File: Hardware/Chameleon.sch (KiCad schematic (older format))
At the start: 59 parts, among them IC1 ATTINY44-SS, P1 CONN_3X2, U1 PCA9685, U2 USBMICRO-B, U3 NCP1402, X1 CRYSTAL

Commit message: Added I2C series resistors, updated Project Log, added PDF version of Project Log
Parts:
- added R22, R3: 1.5k, symbol R
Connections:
- wire segments 236 -> 238
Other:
- moved on the sheet: R1, R2

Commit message: Updated schematics and Project Log with new resistor values, and added PDF BOM
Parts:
- R1, R2: value 1.5k -> 1.8k
- R22, R3: value 1.5k -> 100
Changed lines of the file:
@@
-EESchema Schematic File Version 2  date 8/27/2012 9:40:04 PM
+EESchema Schematic File Version 2  date 9/9/2012 6:02:59 PM
 LIBS:power
 LIBS:device
@@
 Sheet 1 1
 Title "Chameleon Drink Coasters"
-Date "28 aug 2012"
+Date "9 sep 2012"
 Rev "1.0"
 Comp "Projects and Stuff LLC"
@@
 P 950 5550
 F 0 "R3" V 1050 5550 50  0000 C CNN
-F 1 "1.5k" V 950 5550 50  0000 C CNN
+F 1 "100" V 950 5550 50  0000 C CNN
 	1    950  5550
 	0    1    1    0
@@
 P 1000 5450
 F 0 "R22" V 1080 5450 50  0000 C CNN
-F 1 "1.5k" V 1000 5450 50  0000 C CNN
+F 1 "100" V 1000 5450 50  0000 C CNN
 	1    1000 5450
 	0    -1   -1   0
@@
 P 1300 5050
 F 0 "R1" V 1380 5050 50  0000 C CNN
-F 1 "1.5k" V 1300 5050 50  0000 C CNN
+F 1 "1.8k" V 1300 5050 50  0000 C CNN
 	1    1300 5050
 	-1   0    0    1
@@
 P 1450 5050
 F 0 "R2" V 1530 5050 50  0000 C CNN
-F 1 "1.5k" V 1450 5050 50  0000 C CNN
+F 1 "1.8k" V 1450 5050 50  0000 C CNN
 	1    1450 5050
 	-1   0    0    1
@@
 6E 56 52 49 51 4E 59 71 7E 65 C5 4D 0F AF 00 BF F6 21 9D BA 45 88 9C 00 16 00 C0 66 90 E0 00 00
 AC 42 3B 38 00 00 AB 90 E0 00 00 AC 42 82 03 00 B0 EA FF 00 E3 76 B5 A7 81 B6 BC 08 00 00 00 00
-49 45 4E 44 AE 42 60 82 4E $EndBitmap
+49 45 4E 44 AE 42 60 82 38 $EndBitmap
 EndData
 $EndBitmap

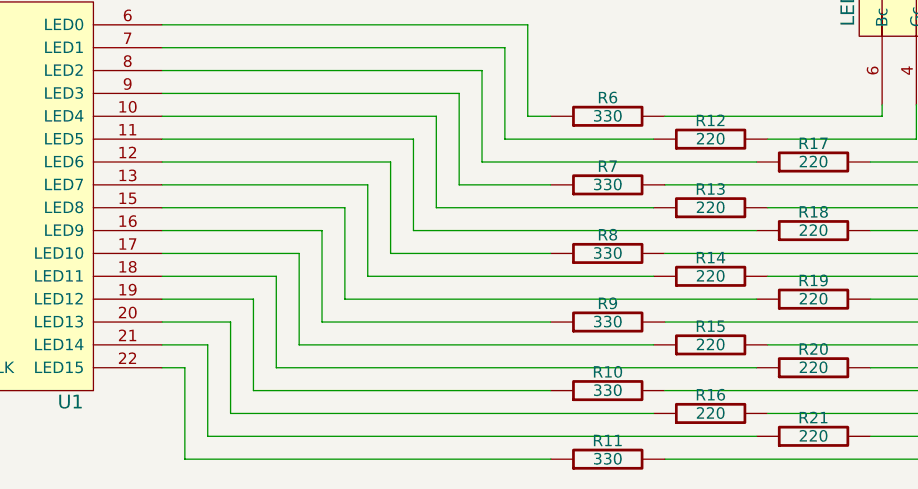
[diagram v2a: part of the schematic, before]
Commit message: Routed board (with LEDs corrected) and updated Project Log
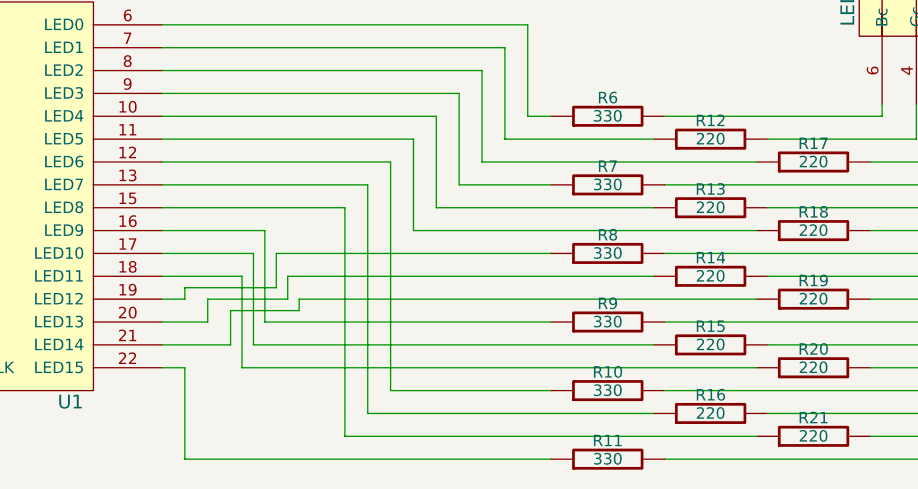
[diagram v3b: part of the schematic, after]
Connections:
- wire segments 238 -> 244
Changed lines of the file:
@@
-EESchema Schematic File Version 2  date 9/9/2012 6:02:59 PM
+EESchema Schematic File Version 2  date 12/30/2012 6:35:34 PM
 LIBS:power
 LIBS:device
@@
 Sheet 1 1
 Title "Chameleon Drink Coasters"
-Date "9 sep 2012"
+Date "30 dec 2012"
 Rev "1.0"
 Comp "Projects and Stuff LLC"
@@
 $EndDescr
 Wire Wire Line
+	4700 6850 3100 6850
+Wire Wire Line
+	5600 6750 3800 6750
+Wire Wire Line
+	3800 6750 3800 5750
+Wire Wire Line
+	3800 5750 3000 5750
+Wire Wire Line
+	3000 5550 4000 5550
+Wire Wire Line
+	4000 5550 4000 6550
+Wire Wire Line
+	4000 6550 4700 6550
+Wire Wire Line
+	5150 6050 3550 6050
+Wire Wire Line
+	3550 6050 3550 6150
+Wire Wire Line
+	3550 6150 3200 6150
+Wire Wire Line
+	3200 6150 3200 6250
+Wire Wire Line
+	5600 6450 3350 6450
+Wire Wire Line
+	3350 6450 3350 6050
+Wire Wire Line
+	3350 6050 3000 6050
+Wire Wire Line
+	3000 5850 3450 5850
+Wire Wire Line
+	3450 5850 3450 6250
+Wire Wire Line
+	3450 6250 4700 6250
+Wire Wire Line
+	3000 6150 3100 6150
+Wire Wire Line
 	600  5550 700  5550
 Wire Wire Line
@@
 	1700 6250 1750 6250
 Wire Wire Line
-	3000 6450 3100 6450
-Wire Wire Line
-	3100 6450 3100 6850
-Wire Wire Line
-	3100 6850 4700 6850
-Wire Wire Line
 	10300 3600 10300 4500
 Wire Wire Line
@@
 	6300 5450 5650 5450
 Wire Wire Line
-	3000 6050 3500 6050
-Wire Wire Line
-	3000 5850 3700 5850
-Wire Wire Line
-	3000 5650 3900 5650
-Wire Wire Line
 	3000 5450 4100 5450
 Wire Wire Line
@@
 Wire Wire Line
 	3000 5050 4500 5050
-Wire Wire Line
-	3000 6150 3400 6150
-Wire Wire Line
-	3000 6350 3200 6350
-Wire Wire Line
-	3300 6650 3300 6250
-Wire Wire Line
-	3300 6650 5150 6650
-Wire Wire Line
-	3500 6050 3500 6450
-Wire Wire Line
-	3500 6450 5600 6450
-Wire Wire Line
-	3700 5850 3700 6250
-Wire Wire Line
-	3700 6250 4700 6250
-Wire Wire Line
-	5150 6050 3900 6050
-Wire Wire Line
-	3900 6050 3900 5650
 Wire Wire Line
 	5600 5850 4100 5850
@@
 	4200 5750 5150 5750
 Wire Wire Line
-	4000 5950 4000 5550
-Wire Wire Line
-	4000 5950 4700 5950
-Wire Wire Line
-	3800 6150 3800 5750
-Wire Wire Line
-	3800 6150 5600 6150
-Wire Wire Line
-	5150 6350 3600 6350
-Wire Wire Line
-	3600 6350 3600 5950
-Wire Wire Line
-	4700 6550 3400 6550
-Wire Wire Line
-	3400 6550 3400 6150
-Wire Wire Line
-	5600 6750 3200 6750
-Wire Wire Line
-	3200 6750 3200 6350
-Wire Wire Line
-	3300 6250 3000 6250
-Wire Wire Line
 	4600 4950 3000 4950
 Wire Wire Line
@@
 Wire Wire Line
 	4200 5350 3000 5350
-Wire Wire Line
-	4000 5550 3000 5550
-Wire Wire Line
-	3800 5750 3000 5750
-Wire Wire Line
-	3600 5950 3000 5950
 Wire Wire Line
 	6150 5350 5200 5350
@@
 Wire Wire Line
 	1200 5550 1750 5550
+Wire Wire Line
+	3200 6250 3000 6250
+Wire Wire Line
+	3000 6350 3300 6350
+Wire Wire Line
+	3000 5950 3400 5950
+Wire Wire Line
+	3400 5950 3400 6350
+Wire Wire Line
+	3400 6350 5150 6350
+Wire Wire Line
+	4700 5950 3500 5950
+Wire Wire Line
+	3500 5950 3500 6100
+Wire Wire Line
+	3500 6100 3100 6100
+Wire Wire Line
+	3100 6100 3100 6150
+Wire Wire Line
+	3300 6350 3300 6200
+Wire Wire Line
+	3300 6200 3600 6200
+Wire Wire Line
+	3600 6200 3600 6150
+Wire Wire Line
+	3600 6150 5600 6150
+Wire Wire Line
+	5150 6650 3900 6650
+Wire Wire Line
+	3900 6650 3900 5650
+Wire Wire Line
+	3900 5650 3000 5650
+Wire Wire Line
+	3100 6850 3100 6450
+Wire Wire Line
+	3100 6450 3000 6450
 Text Label 600  5550 1    60   ~ 0
 MOSI
@@
 6E 56 52 49 51 4E 59 71 7E 65 C5 4D 0F AF 00 BF F6 21 9D BA 45 88 9C 00 16 00 C0 66 90 E0 00 00
 AC 42 3B 38 00 00 AB 90 E0 00 00 AC 42 82 03 00 B0 EA FF 00 E3 76 B5 A7 81 B6 BC 08 00 00 00 00
-49 45 4E 44 AE 42 60 82 38 $EndBitmap
+49 45 4E 44 AE 42 60 82 89 $EndBitmap
 EndData
 $EndBitmap

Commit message: Began transitioning to updated Parts to improve function and increase capability.
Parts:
- removed C4, C5: 8pF, symbol CSMALL
- removed X1: CRYSTAL, symbol CRYSTAL
- added F?: FUSE, ~, symbol FUSE
- added IC?: ATXMEGA16A4U-A, TQFP44, symbol ATXMEGA16A4U-A
- P1: value CONN_3X2 -> PDI
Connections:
- net labels added: D+, D-
- wire segments 244 -> 284
- no-connect marks 4 -> 2
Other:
- note added: "Due to the XMEGA dedicated\nSerial ports, these resistors\nno longer required"
- note added: "Need to replace with water\nresistant right-angle\npush-button switches"
- note added: "Replace with AS1121\nNegates the need for\ncurrent limiting resistors"
- note added: "Replace with an SC560B/C\nDual Output LDO"
- note removed: "Crystal and Load Caps"
- moved on the sheet: BT1, D1, L2, P1, RX0, RY0, RYB0, TP1, TP2, U2, U3

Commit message: Made a number of notes in the schematics based on new knowledge and past mistakes.
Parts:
- F?: value FUSE -> PTC FUSE
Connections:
- net labels added: PDI_CLK, PDI_DATA, SW?
- wire segments 284 -> 282
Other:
- note added: "Import smaller RGB LED\nfrom Pong.0"
- note added: "Need to replace with\nwater resistant right-angle\npush-button switches"
- note added: "Part should be specified\n(ZX62WRD-B-5PC). Water\nresistant USB Micro. Also,\nUSB Shield should be properly\nterminated."
- note added: "Remove ATTiny44"
- note added: "Switches"
- note added: "These bypass caps\nshould be 1nF. Verify\nin the QMatrix App Notes"
- note added: "Update with PDI Header pins"
- note added: "Use proper nomenclature\nfor LEDs. IE: D1, D2, Dn"
- note added: "VCC here is 5V, but QMatrix is\ndesigned for lower voltage. 5V\nis too high for reliable operation."
- note removed: "Need to replace with water\nresistant right-angle\npush-button switches"
- moved on the sheet: BT1, D1, F?, L2, P1, R4, R5, RX0, RY0, RYB0, S1, S2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

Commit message: Made major updates to power management and control
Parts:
- removed C1, C2: .1uF, symbol CSMALL
- removed C14: 10uF, symbol CSMALL
- removed IC1: ATTINY44-SS, SO14, symbol ATTINY44-SS
- removed L1: 33uH, symbol INDUCTOR
- removed R1, R2: 1.8k, symbol R
- removed R10, R11, R6, R7, R8, R9: 330, symbol R
- removed R12, R13, R14, R15, R16, R17, R18, R19, R20, R21: 220, symbol R
- removed R22, R3: 100, symbol R
- removed U1: PCA9685, symbol PCA9685
- added C? (x2): 0.1uF, ~, symbol CSMALL
- added R? (x4): 10k, ~, symbol R
- added R?: 4k, ~, symbol R
- added U?: TLV71333PDBVR, SOT-23-5, symbol TLV71333PDBVR
- added U?: AS1121, symbol AS1121
- C10, C11, C13, C6, C7, C8: value .1uF -> 1nF
- D7: renamed from D1; value DIODESCH_MOD -> ZLLS410TA
- renumbered LED1 to D1, LED2 to D2, LED3 to D3, LED4 to D4, LED5 to D5, D2 to D6
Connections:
- net labels added: GSCLK, OEN, P2_EN, PD, VLED, XERR, ~SS~
- net labels removed: RESET, XTAL1, XTAL2
- wire segments 282 -> 218
- no-connect marks 2 -> 5
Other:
- note added: "PDI Header"
- note added: "Pulls high to initially\nturn AS1121 off"
- note added: "Pulls high to initially\nturn outputs off"
- note added: "Pulls low to initially\nset to Grayscale mode"
- note removed: "Due to the XMEGA dedicated\nSerial ports, these resistors\nno longer required"
- note removed: "ISP Header"
- note removed: "Remove ATTiny44"
- note removed: "Replace with AS1121\nNegates the need for\ncurrent limiting resistors"
- note removed: "Replace with an SC560B/C\nDual Output LDO"
- note removed: "These bypass caps\nshould be 1nF. Verify\nin the QMatrix App Notes"
- note removed: "Use proper nomenclature\nfor LEDs. IE: D1, D2, Dn"
- note removed: "VCC here is 5V, but QMatrix is\ndesigned for lower voltage. 5V\nis too high for reliable operation."
- moved on the sheet: BT1, D1, D2, D3, D4, D5, D6, D7, F?, IC?, L2, P1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
